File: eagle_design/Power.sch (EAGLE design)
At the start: 17 parts, among them K1 G5LE, K2 G5LE, K3 G5LE

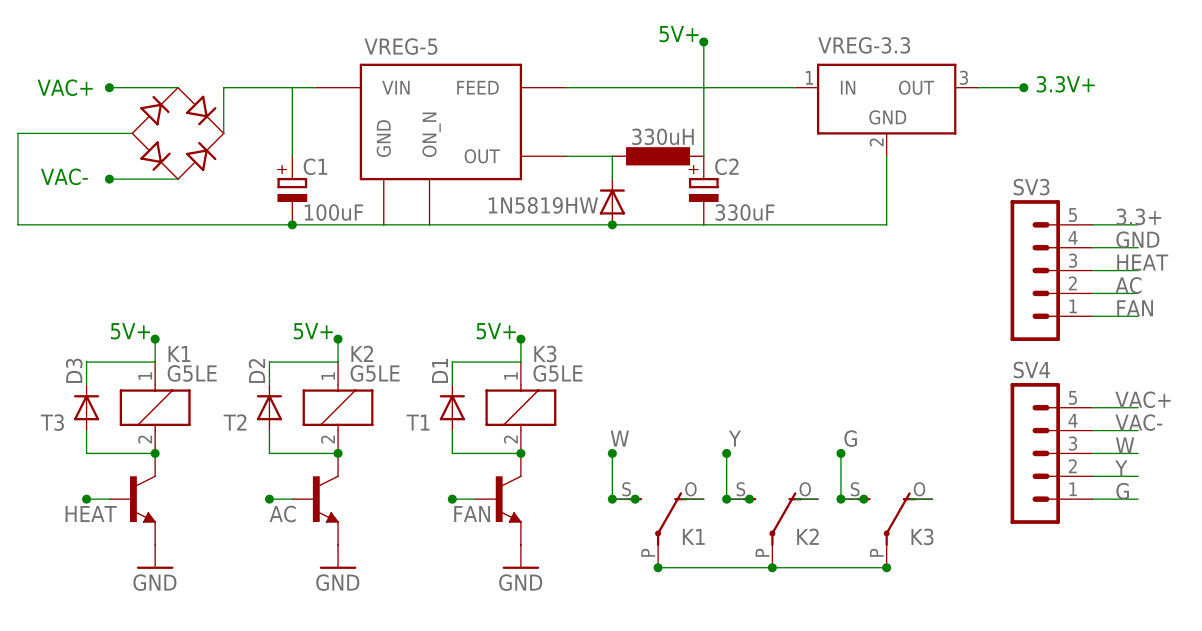
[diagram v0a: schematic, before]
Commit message: split into three boards and choose new mcu
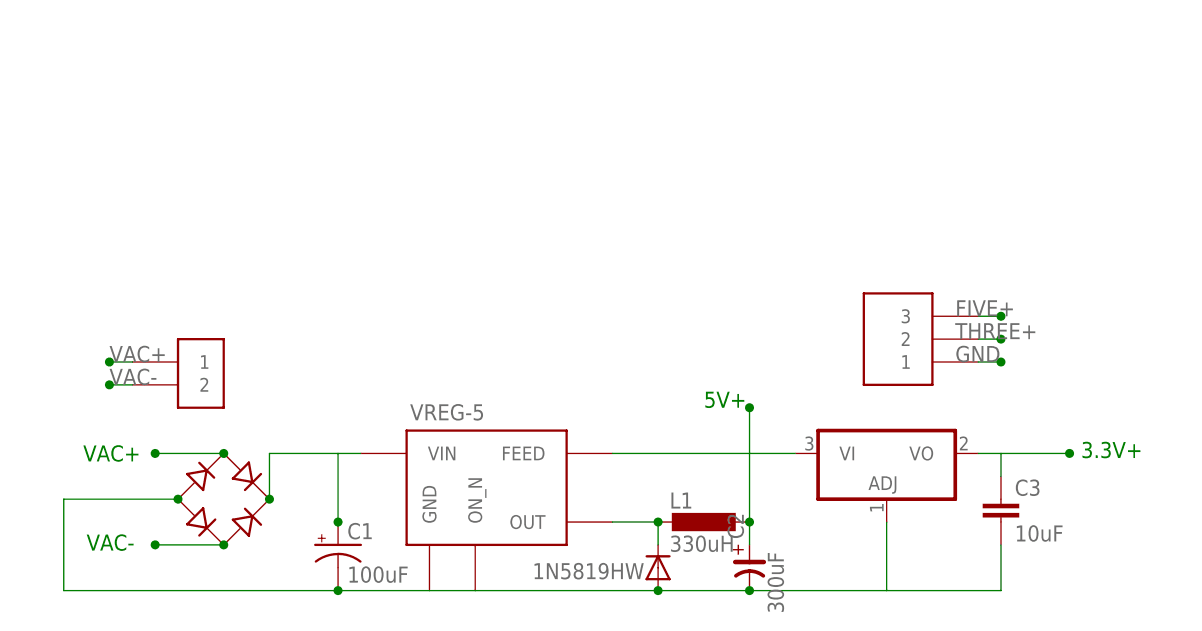
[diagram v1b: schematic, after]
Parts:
- removed D1, D2, D3: 1N4148DO35-7, diode:1N4148DO35-7
- removed K1, K2, K3: G5LE, relay:G5LE
- removed SV3, SV4: (no value), con-lstb:MA05-1
- removed T1, T2, T3: (no value), transistor-neu-to92:2N4401-NPN-TO92-EBC
- removed VREG-3.3: (no value), linear-technology:LT1129CST5
- added C3: 10uF, capacitor-wima:C5/2.5
- added L1: 330uH, TylersLib:DO3316P
- added LT1086-3.3: 317T, linear:317T
- added U$1: SCREWTERMINAL-3, SparkFun-Connectors:SCREWTERMINAL-3
- added U$2: SCREWTERMINAL-2, SparkFun-Connectors:SCREWTERMINAL-2
- C1: device rcl:CPOL-EU153CLV-0405 -> rcl:CPOL-USG
- C2: value 330uF -> 300uF; device rcl:CPOL-EU153CLV-0405 -> rc-master:CP_SV-H
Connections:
- net N$1 renamed VUNREG
- removed net 3.3+: SV3.5, VREG-3.3G$1.OUT
- removed net 5V+: C2.+, D1.C, D2.C, D3.C, K11.1, K21.1, K31.1, VREG-3.3G$1.IN, VREG-5.FEED
- removed net AC: SV3.2, T2.B
- removed net FAN: SV3.1, T1.B
- removed net G: K32.S, SV4.1
- removed net HEAT: SV3.3, T3.B
- removed net N$2: D1.A, K31.2, T1.C
- removed net N$3: D2.A, K21.2, T2.C
- removed net N$5: D3.A, K11.2, T3.C
- removed net N$6: K12.O
- removed net N$7: K22.O
- removed net N$8: K32.O
- removed net W: K12.S, SV4.3
- removed net Y: K22.S, SV4.2
- new net FIVE+: C2.+, L1.2, LT1086-3.3.VI, U$1.3, VREG-5.FEED
- new net THREE+: C3.1, LT1086-3.3.VO, U$1.2
- net GND: now also C3.2, LT1086-3.3.ADJ, U$1.1; no longer SV3.4, T1.E, T2.E, T3.E, VREG-3.3G$1.GND
- net N$4: now also L1.1
- net VAC+: now also U$2.1; no longer K12.P, K22.P, K32.P, SV4.5
- net VAC-: now also B1.AC2, U$2.2; no longer SV4.4
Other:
- note removed: "330uH"
- note removed: "G"
- note removed: "W"
- note removed: "Y"
- moved on the sheet: C1, C2

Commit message: made boards smaller
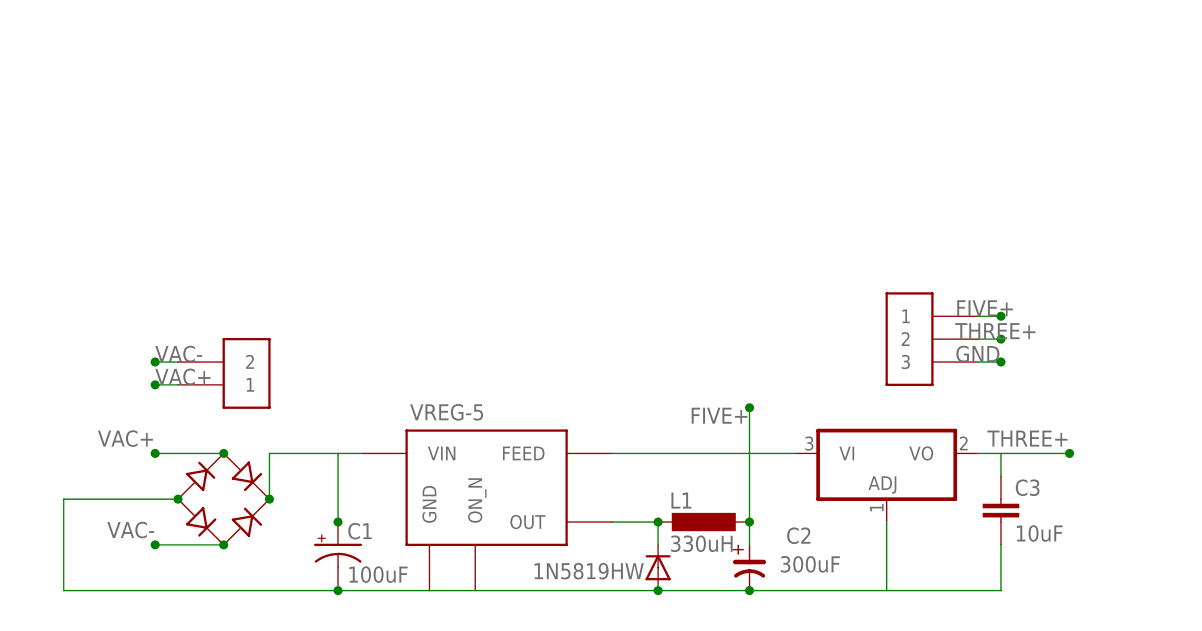
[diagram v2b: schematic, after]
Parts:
- removed U$1: SCREWTERMINAL-3, SparkFun-Connectors:SCREWTERMINAL-3
- added U$3: OSTTC030162, TylersLib:OSTTC030162
- U$2: value SCREWTERMINAL-2 -> OSTTC020162; device SparkFun-Connectors:SCREWTERMINAL-2 -> TylersLib:OSTTC020162
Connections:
- net FIVE+: now also U$3.1; no longer U$1.3
- net GND: now also U$3.3; no longer U$1.1
- net THREE+: now also U$3.2; no longer U$1.2
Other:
- note removed: "3.3V+"
- note removed: "5V+"
- note removed: "VAC+"
- note removed: "VAC-"
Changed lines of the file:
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@@
 <part name="C3" library="capacitor-wima" deviceset="C" device="5/2.5" value="10uF"/>
 <part name="L1" library="TylersLib" deviceset="DO3316P" device="" value="330uH"/>
-<part name="U$1" library="SparkFun-Connectors" deviceset="SCREWTERMINAL-3" device=""/>
-<part name="U$2" library="SparkFun-Connectors" deviceset="SCREWTERMINAL-2" device=""/>
+<part name="U$2" library="TylersLib" deviceset="OSTTC020162" device=""/>
+<part name="U$3" library="TylersLib" deviceset="OSTTC030162" device=""/>
 </parts>
 <sheets>
@@
 <plain>
 <text x="38.481" y="18.923" size="1.778" layer="95">VREG-5</text>
-<text x="2.159" y="14.351" size="1.778" layer="91">VAC+</text>
-<text x="2.54" y="4.445" size="1.778" layer="91">VAC-</text>
-<text x="71.12" y="20.32" size="1.778" layer="91">5V+</text>
-<text x="113.03" y="14.732" size="1.778" layer="91">3.3V+</text>
 <text x="52.07" y="1.27" size="1.778" layer="95">1N5819HW</text>
 </plain>
@@
 <instance part="B1" gate="G$1" x="17.78" y="10.16" smashed="yes"/>
 <instance part="C1" gate="G$1" x="30.48" y="5.08"/>
-<instance part="C2" gate="G$1" x="76.2" y="2.54" rot="R90"/>
+<instance part="C2" gate="G$1" x="76.2" y="2.54" smashed="yes" rot="R90">
+<attribute name="NAME" x="83.185" y="6.985" size="1.778" layer="95" rot="R180"/>
+<attribute name="VALUE" x="86.36" y="3.81" size="1.778" layer="96" rot="R180"/>
+</instance>
 <instance part="LT1086-3.3" gate="A1" x="91.44" y="12.7" smashed="yes"/>
 <instance part="C3" gate="G$1" x="104.14" y="10.16"/>
 <instance part="L1" gate="G$1" x="71.12" y="7.62"/>
-<instance part="U$1" gate="G$1" x="96.52" y="22.86" rot="R90"/>
-<instance part="U$2" gate="G$1" x="12.7" y="27.94" rot="R270"/>
+<instance part="U$2" gate="G$1" x="22.86" y="27.94" rot="R180"/>
+<instance part="U$3" gate="G$1" x="96.52" y="22.86"/>
 </instances>
 <busses>
@@
 </segment>
 <segment>
-<pinref part="U$1" gate="G$1" pin="1"/>
 <wire x1="101.6" y1="25.4" x2="104.14" y2="25.4" width="0.1524" layer="91"/>
 <junction x="104.14" y="25.4"/>
 <label x="99.06" y="25.4" size="1.778" layer="95"/>
+<pinref part="U$3" gate="G$1" pin="3"/>
 </segment>
 </net>
@@
 <pinref part="B1" gate="G$1" pin="AC2"/>
 <junction x="17.78" y="5.08"/>
+<label x="10.16" y="7.62" size="1.778" layer="95" rot="R180"/>
 </segment>
 <segment>
 <pinref part="U$2" gate="G$1" pin="2"/>
-<wire x1="7.62" y1="22.86" x2="5.08" y2="22.86" width="0.1524" layer="91"/>
-<junction x="5.08" y="22.86"/>
-<label x="5.08" y="22.86" size="1.778" layer="95"/>
+<wire x1="12.7" y1="25.4" x2="10.16" y2="25.4" width="0.1524" layer="91"/>
+<junction x="10.16" y="25.4"/>
+<label x="10.16" y="25.4" size="1.778" layer="95"/>
 </segment>
 </net>
@@
 <pinref part="B1" gate="G$1" pin="AC1"/>
 <junction x="17.78" y="15.24"/>
+<label x="10.16" y="17.78" size="1.778" layer="95" rot="R180"/>
 </segment>
 <segment>
 <pinref part="U$2" gate="G$1" pin="1"/>
-<wire x1="7.62" y1="25.4" x2="5.08" y2="25.4" width="0.1524" layer="91"/>
-<junction x="5.08" y="25.4"/>
-<label x="5.08" y="25.4" size="1.778" layer="95"/>
+<wire x1="12.7" y1="22.86" x2="10.16" y2="22.86" width="0.1524" layer="91"/>
+<junction x="10.16" y="22.86"/>
+<label x="10.16" y="22.86" size="1.778" layer="95"/>
 </segment>
 </net>
@@
 <net name="FIVE+" class="0">
 <segment>
-<pinref part="U$1" gate="G$1" pin="3"/>
 <wire x1="101.6" y1="30.48" x2="104.14" y2="30.48" width="0.1524" layer="91"/>
 <junction x="104.14" y="30.48"/>
 <label x="99.06" y="30.48" size="1.778" layer="95"/>
+<pinref part="U$3" gate="G$1" pin="1"/>
 </segment>
 <segment>
@@
 <pinref part="L1" gate="G$1" pin="2"/>
 <junction x="76.2" y="7.62"/>
+<label x="76.2" y="20.32" size="1.778" layer="95" rot="R180"/>
 </segment>
 </net>
@@
 <wire x1="104.14" y1="15.24" x2="111.76" y2="15.24" width="0.1524" layer="91"/>
 <wire x1="104.14" y1="12.7" x2="104.14" y2="15.24" width="0.1524" layer="91"/>
+<label x="111.76" y="17.78" size="1.778" layer="95" rot="R180"/>
 </segment>
 <segment>
-<pinref part="U$1" gate="G$1" pin="2"/>
 <wire x1="101.6" y1="27.94" x2="104.14" y2="27.94" width="0.1524" layer="91"/>
 <junction x="104.14" y="27.94"/>
 <label x="99.06" y="27.94" size="1.778" layer="95"/>
+<pinref part="U$3" gate="G$1" pin="2"/>
 </segment>
 </net>
